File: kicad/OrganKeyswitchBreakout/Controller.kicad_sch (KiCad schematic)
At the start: 13 parts, among them SW1 MODES, U2 ESP32-S3-DevKitC

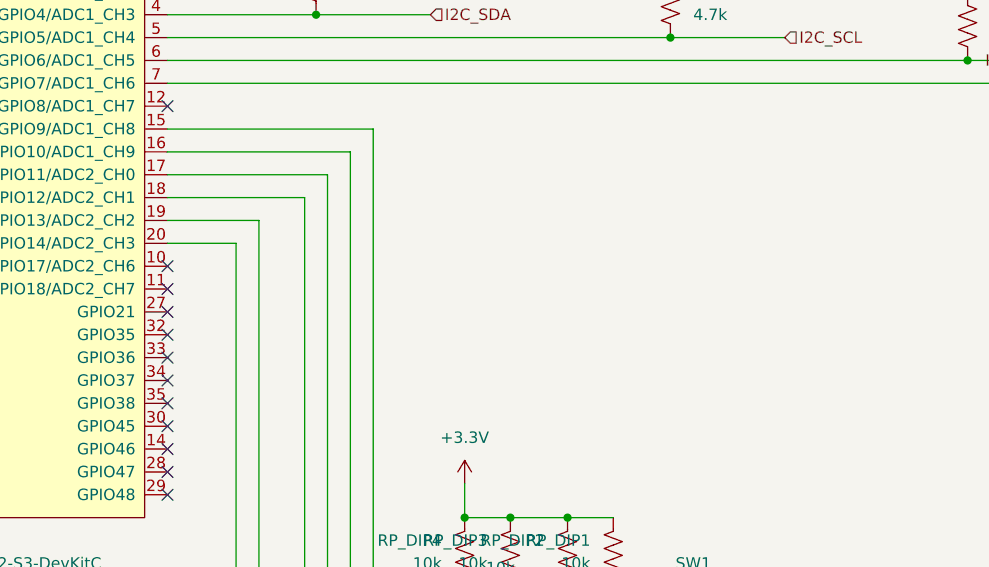
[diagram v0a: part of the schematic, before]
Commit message: Adding keyswitch breakout system, and some tools
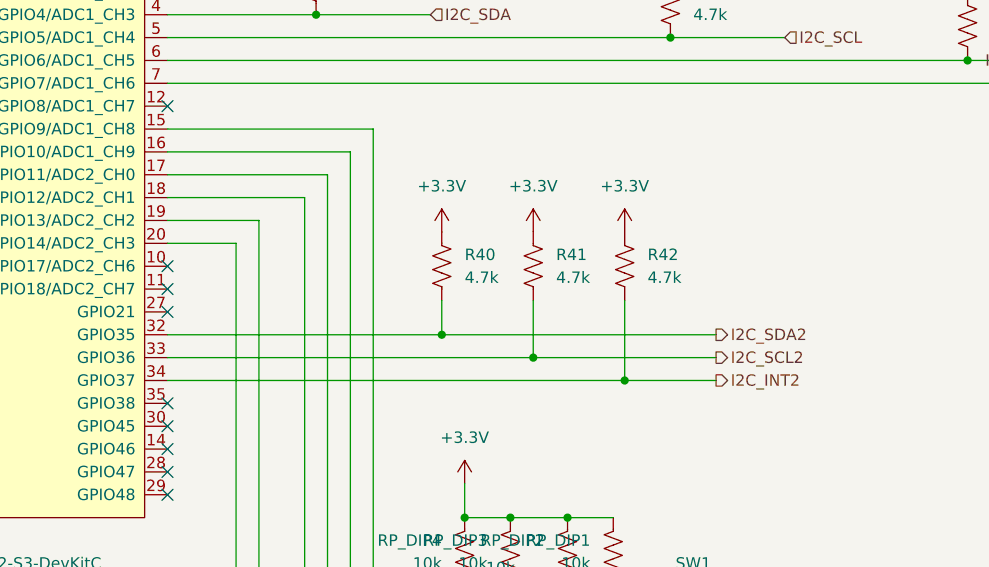
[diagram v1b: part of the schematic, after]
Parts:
- added R40, R41, R42: 4.7k, Resistor_SMD:R_0805_2012Metric, symbol Device:R_US
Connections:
- net +3.3V: now also R40.1, R41.1, R42.1
- net I2C_SDA2: now reaches U2.32 (GPIO35)
- net I2C_SDA2: now also R40.2
- net I2C_SCL2: now reaches U2.33 (GPIO36)
- net I2C_SCL2: now also R41.2
- net I2C_INT2: now reaches U2.34 (GPIO37)
- net I2C_INT2: now also R42.2
- no-connect marks 25 -> 22
